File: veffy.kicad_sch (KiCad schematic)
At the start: 121 parts, among them CN1 XH-2AW_C2908611, J1 SWD, J2 Conn_Coaxial, J3 USB_C_Receptacle_USB2.0_14P, Q1 2N7002, Q2 BFR93A, Q3 2N7002, Q4 BFR93AE6327HTSA1, SW1 SW_Push, U1 ATSAMD21G18A-A, U2 ADF4112BCPZ, U3 SA612AN/01_112, U4 MC3361, U5 LM386, U6 LM358_DFN, U7 AD9834, U8 QPA9510, U9 MCP73831-2-OT, Y2 TCXO-14

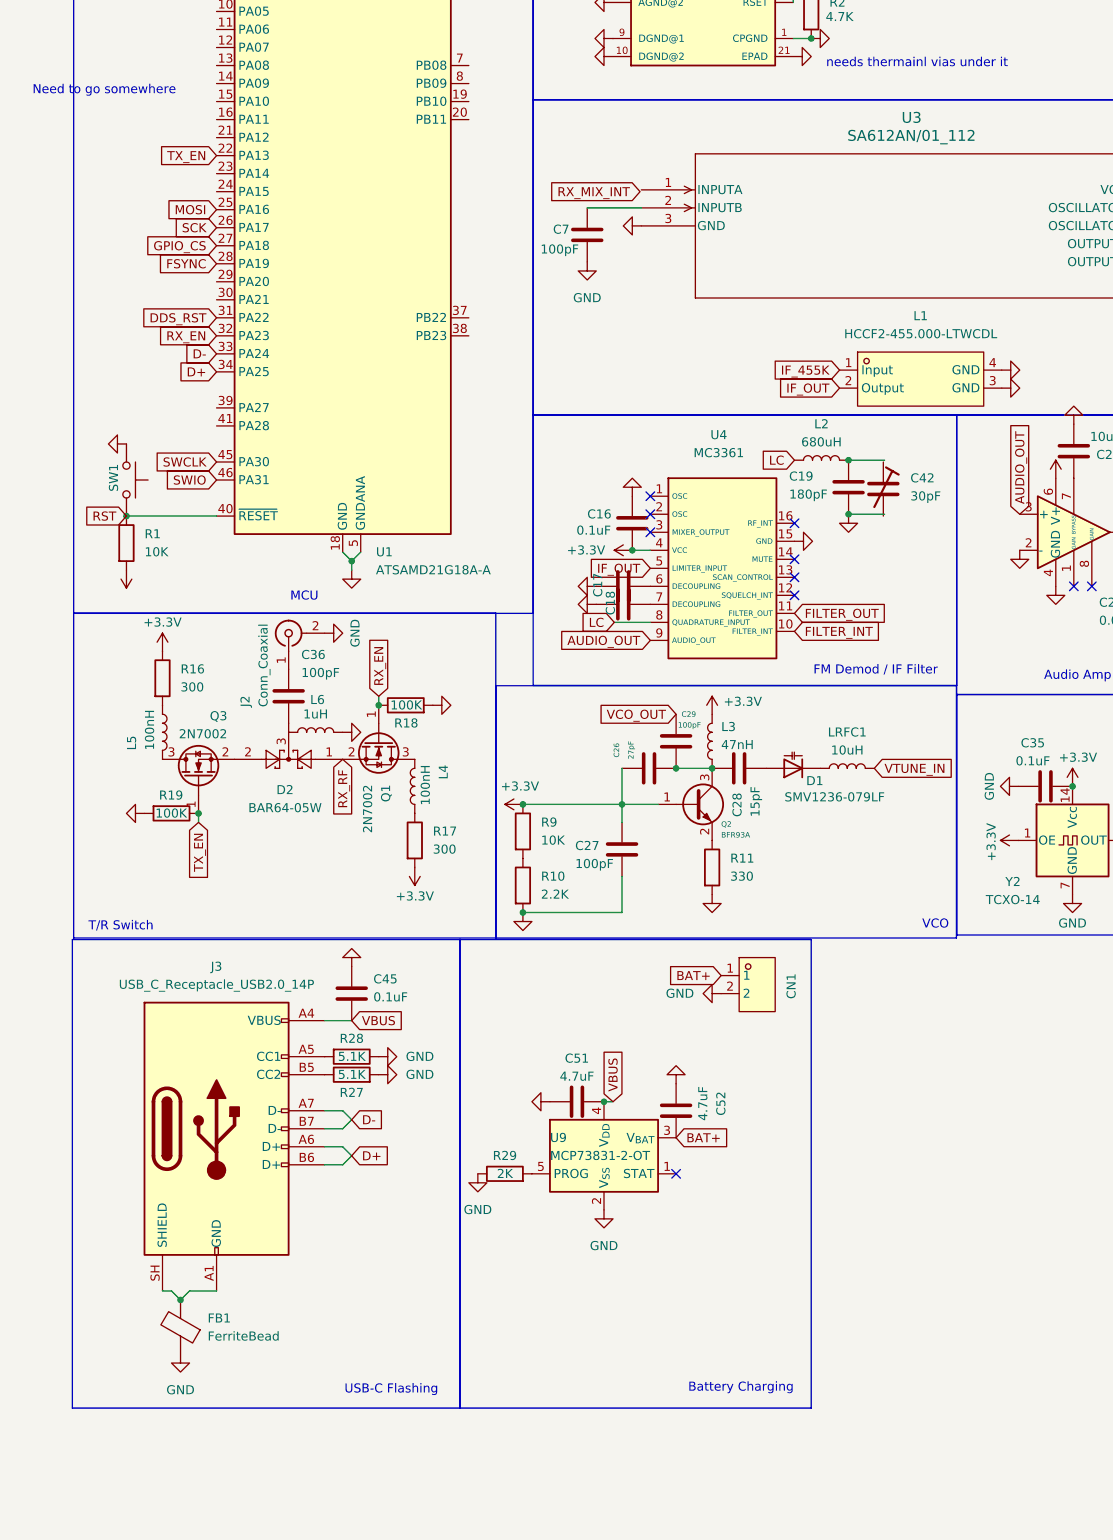
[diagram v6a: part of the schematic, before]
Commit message: boost converter
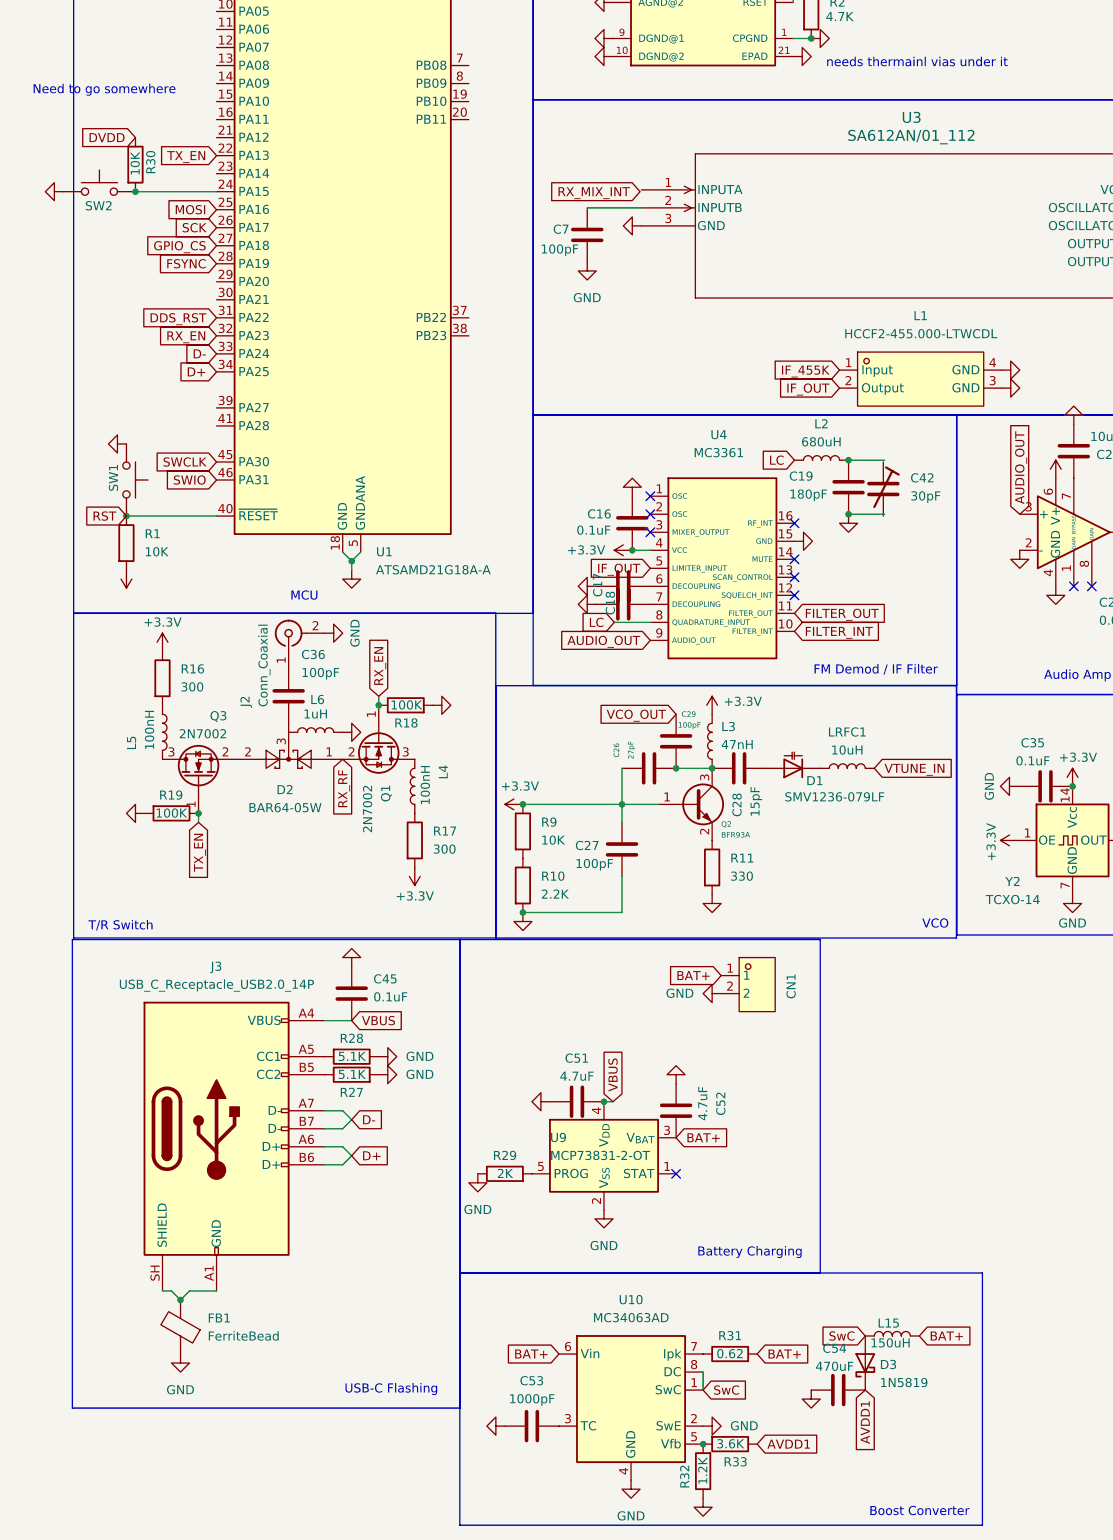
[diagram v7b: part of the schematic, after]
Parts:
- added C53: 1000pF, symbol Device:C
- added C54: 470uF, symbol Device:C
- added D3: 1N5819, Diode_THT:D_DO-41_SOD81_P10.16mm_Horizontal, symbol Diode:1N5819
- added L15: 150uH, symbol Device:L
- added R30: 10K, symbol Device:R
- added R31: 0.62, symbol Device:R
- added R32: 1.2K, symbol Device:R
- added R33: 3.6K, symbol Device:R
- added SW2: SW_Push, symbol Switch:SW_Push
- added U10: MC34063AD, Package_SO:SOIC-8_3.9x4.9mm_P1.27mm, symbol Regulator_Switching:MC34063AD
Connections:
- net +3.3V: now also R30.1
- net +5V: now also C54.2, D3.1 (K), R33.1
- net BAT+: now also L15.2, R31.2, U10.6 (Vin)
- net GND: now also C53.1, C54.1, R32.1, SW2.1, U10.2 (SwE), U10.4 (GND)
- net at U1.24 (PA15): now also R30.2, SW2.2
- new net: C53.2, U10.3 (TC)
- new net: R32.2, R33.2, U10.5 (Vfb)
- new net: R31.1, U10.7 (Ipk)
- new net SwC: D3.2 (A), L15.1, U10.1 (SwC), U10.8 (DC)
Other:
- note added: "Boost Converter"

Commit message: uuh, idr what I added. I think the LDO
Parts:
- added C55, C56: 1uF, symbol Device:C
- added U11: AP2112K-3.3, Package_TO_SOT_SMD:SOT-23-5, symbol Regulator_Linear:AP2112K-3.3
- Y2: value TCXO-14 -> C7527392; footprint Oscillator:Oscillator_DIP-14 -> OSC-SMD_4P-L2.0-W1.6-BL_EPSON_TG-5006CJ-19H
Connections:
- net +3.3V: now also C56.2, U11.5 (VOUT)
- net BAT+: now also C55.2, U11.1 (VIN), U11.3 (EN)
- net GND: now also C55.1, C56.1, U11.2 (GND)
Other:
- note added: "LOD - 3.3V"
